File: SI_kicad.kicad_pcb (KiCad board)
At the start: 2 copper layers, 100 x 57 mm, 88 parts, among them J1 Conn_01x16_Female, J2 SCW_TERM_01x02, J3 Conn_02x05_Counter_Clockwise, J4 Conn_01x05_Male, J5 Conn_01x05_Female, J6 Conn_01x02, J7 Conn_01x02, Q1 BC549, Q2 BC557C, Q3 IRL7833, SW1 SW_Push, U1 STM32F103C8Tx, U2 AMS1117-3.3, U3 TPS5430DDA, U4 LM358, Y1 8M

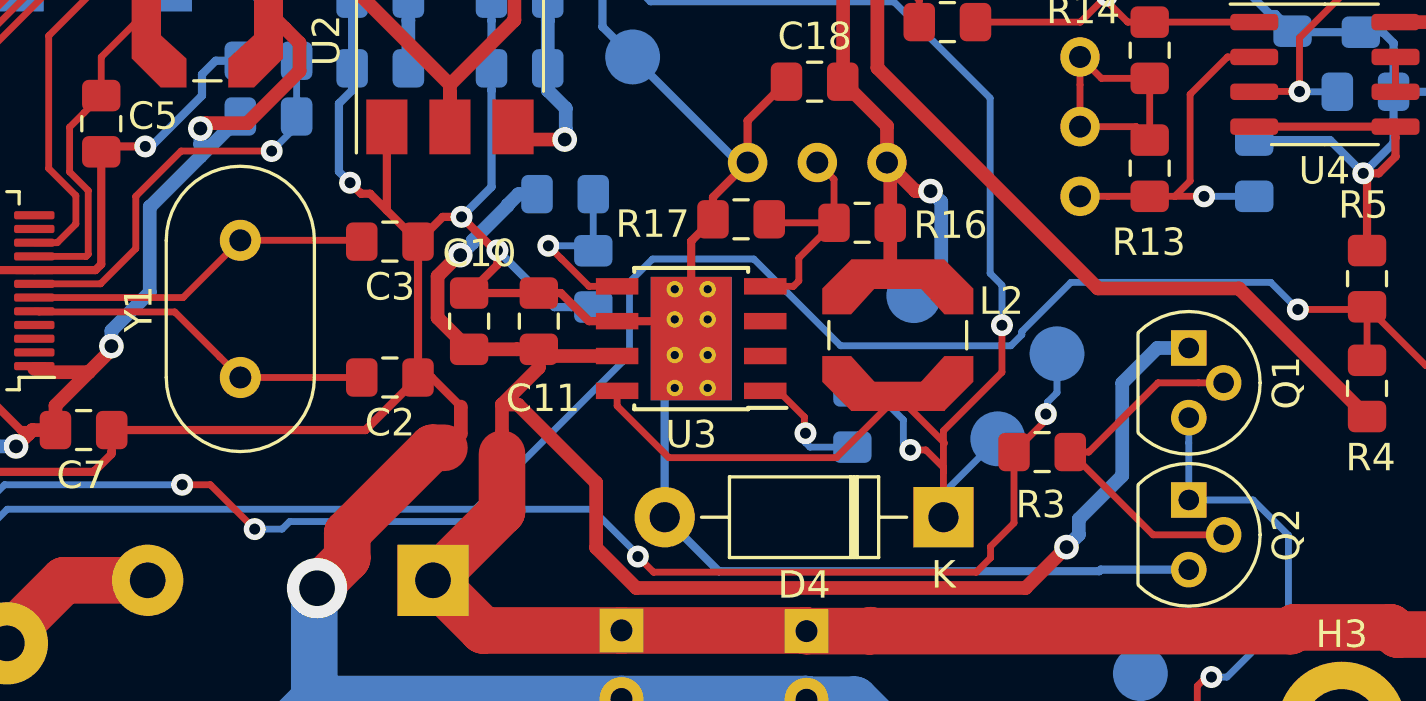
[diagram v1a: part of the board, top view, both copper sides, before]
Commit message: 1.2 Update schematic to kicad 6
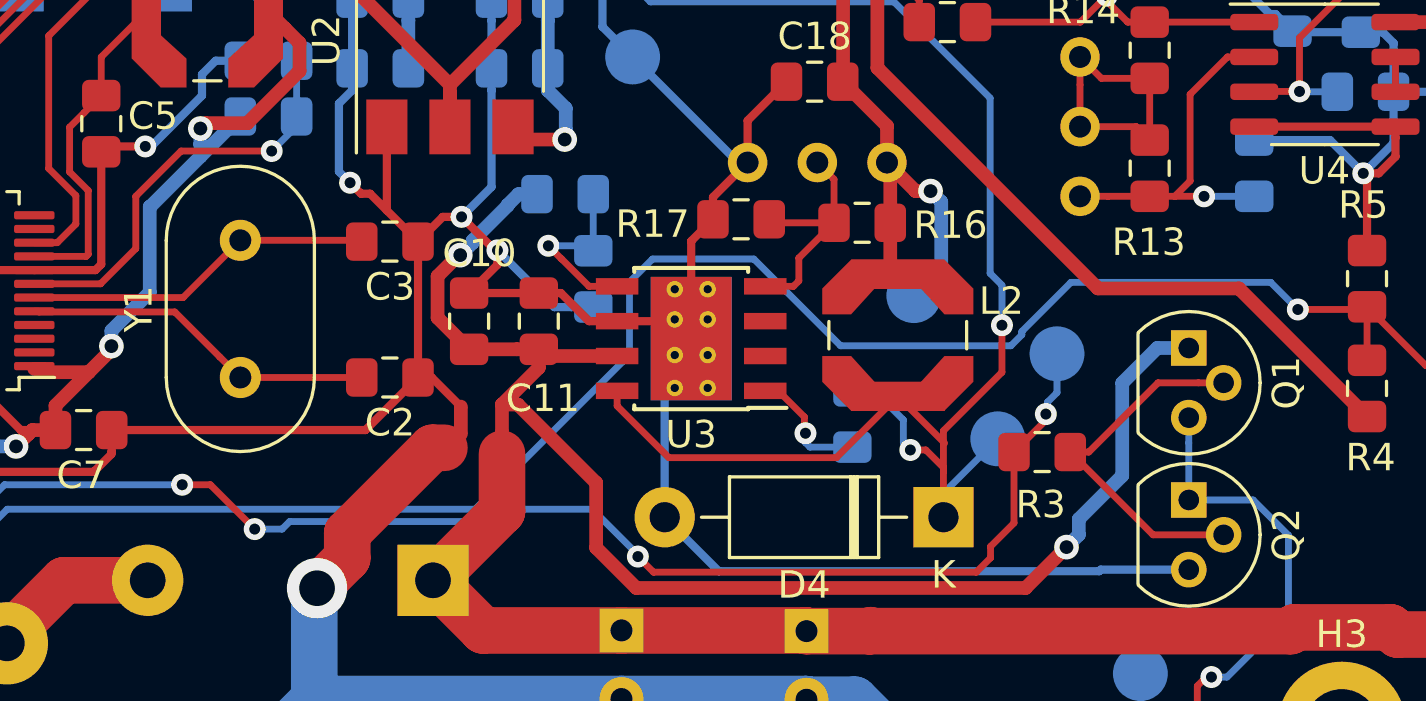
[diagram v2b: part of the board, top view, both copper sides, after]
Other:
- net class +28V removed
- net class Default removed
- net class GND removed
- net class VCC removed

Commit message: 2.0
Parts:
- removed D1: LED, LED_SMD:LED_0805_2012Metric_Pad1.15x1.40mm_HandSolder
- removed L3: INDUCTOR, Inductor_THT:L_Axial_L5.3mm_D2.2mm_P7.62mm_Horizontal_Vishay_IM-1
- removed NT2: Net-Tie_2, NetTie:NetTie-2_SMD_Pad0.5mm
- removed RV1: 1K, Potentiometer_THT:Potentiometer_Bourns_3296W_Vertical
- removed TP1, TP2, TP5, TP6, TP7, TP8, TP9: TestPoint, TestPoint:TestPoint_Pad_D2.0mm
- added C22: 2u, Capacitor_SMD:C_0805_2012Metric_Pad1.18x1.45mm_HandSolder, B.Cu at (103.1, 96.9)
- added C23: C_Polarized, Capacitor_THT:CP_Radial_D6.3mm_P2.50mm, B.Cu at (162.1, 107.5)
- added C24: 10n, Capacitor_SMD:C_0805_2012Metric_Pad1.18x1.45mm_HandSolder, B.Cu at (171.3, 90.4)
- added C25: 100n, Capacitor_SMD:C_0805_2012Metric_Pad1.18x1.45mm_HandSolder, B.Cu at (171.2, 92.2)
- added C26: 4.7u, Capacitor_SMD:CP_Elec_5x5.4, B.Cu at (153.0, 94.2)
- added C27: 100n, Capacitor_SMD:C_0805_2012Metric_Pad1.18x1.45mm_HandSolder, F.Cu at (184.1, 91.6)
- added C28: 100n, Capacitor_SMD:C_0805_2012Metric_Pad1.18x1.45mm_HandSolder, F.Cu at (158.4, 91.6)
- added C29: 100n, Capacitor_SMD:C_0805_2012Metric_Pad1.18x1.45mm_HandSolder, F.Cu at (152.6, 84.2)
- added C30: 100n, Capacitor_SMD:C_0805_2012Metric_Pad1.18x1.45mm_HandSolder, F.Cu at (149.0, 84.2)
- added C31: 10n, Capacitor_SMD:C_0805_2012Metric_Pad1.18x1.45mm_HandSolder, F.Cu at (178.5, 102.2)
- added C32: 100n, Capacitor_SMD:C_0805_2012Metric_Pad1.18x1.45mm_HandSolder, F.Cu at (175.9, 102.3)
- added C33: 10n, Capacitor_SMD:C_0805_2012Metric_Pad1.18x1.45mm_HandSolder, F.Cu at (167.6, 102.2)
- added C34: 100n, Capacitor_SMD:C_0805_2012Metric_Pad1.18x1.45mm_HandSolder, F.Cu at (165.0, 102.2)
- added D5: 1N4001, Diode_SMD:D_SMA, F.Cu at (185.0, 102.5)
- added D6: 1N4001, Diode_SMD:D_SMA, F.Cu at (185.3, 115.1)
- added J10: Conn_01x02, Connector_PinHeader_2.54mm:PinHeader_1x02_P2.54mm_Vertical, B.Cu at (169.9, 82.5)
- added J11: Conn_01x02, Connector_PinHeader_2.54mm:PinHeader_1x02_P2.54mm_Vertical, B.Cu at (162.2, 82.5)
- added J12: Conn_01x02, Connector_PinHeader_2.54mm:PinHeader_1x02_P2.54mm_Vertical, B.Cu at (172.9, 80.0)
- added J13: Conn_01x02, Connector_PinHeader_2.54mm:PinHeader_1x02_P2.54mm_Vertical, B.Cu at (158.9, 80.0)
- added J8: Conn_01x04, Connector_JST:JST_EH_B4B-EH-A_1x04_P2.50mm_Vertical, B.Cu at (99.4, 86.7)
- added J9: Conn_01x04_Female, Connector_JST:JST_EH_B4B-EH-A_1x04_P2.50mm_Vertical, B.Cu at (190.6, 110.5)
- added Q4: 2N7002, Package_TO_SOT_SMD:SOT-23, F.Cu at (110.6, 87.5)
- added Q5: IRL7833, Package_TO_SOT_THT:TO-220-3_Vertical, B.Cu at (176.7, 121.8)
- added Q6: 2N7002, Package_TO_SOT_SMD:SOT-23, F.Cu at (126.0, 149.7)
- added R18: 100R, Resistor_SMD:R_0805_2012Metric_Pad1.20x1.40mm_HandSolder, F.Cu at (146.7, 100.3)
- added R19: 100R, Resistor_SMD:R_0805_2012Metric_Pad1.20x1.40mm_HandSolder, F.Cu at (146.7, 102.9)
- added R20: 100R, Resistor_SMD:R_0805_2012Metric_Pad1.20x1.40mm_HandSolder, F.Cu at (159.1, 100.3)
- added R21: 100R, Resistor_SMD:R_0805_2012Metric_Pad1.20x1.40mm_HandSolder, F.Cu at (159.1, 102.6)
- added R22: 9K, Resistor_SMD:R_0805_2012Metric_Pad1.20x1.40mm_HandSolder, F.Cu at (121.7, 74.9)
- added R23: 100k, Resistor_SMD:R_0805_2012Metric_Pad1.20x1.40mm_HandSolder, F.Cu at (118.5, 83.4)
- added R24: 10k, Resistor_SMD:R_0805_2012Metric_Pad1.20x1.40mm_HandSolder, F.Cu at (167.3, 82.5)
- added R25: 10k, Resistor_SMD:R_0805_2012Metric_Pad1.20x1.40mm_HandSolder, F.Cu at (164.8, 82.5)
- added R26: 100k, Resistor_SMD:R_0805_2012Metric_Pad1.20x1.40mm_HandSolder, F.Cu at (176.1, 82.2)
- added R27: 100k, Resistor_SMD:R_0805_2012Metric_Pad1.20x1.40mm_HandSolder, F.Cu at (155.3, 82.2)
- added R28: 1k, Resistor_SMD:R_0805_2012Metric_Pad1.20x1.40mm_HandSolder, F.Cu at (179.9, 87.7)
- added R29: 1k, Resistor_SMD:R_0805_2012Metric_Pad1.20x1.40mm_HandSolder, F.Cu at (162.5, 87.7)
- added R30: R, Resistor_SMD:R_0805_2012Metric_Pad1.20x1.40mm_HandSolder, F.Cu at (182.0, 91.6)
- added R31: R, Resistor_SMD:R_0805_2012Metric_Pad1.20x1.40mm_HandSolder, F.Cu at (160.5, 91.6)
- added R32: 100k, Resistor_SMD:R_0805_2012Metric_Pad1.20x1.40mm_HandSolder, F.Cu at (179.8, 98.6)
- added R33: 100k, Resistor_SMD:R_0805_2012Metric_Pad1.20x1.40mm_HandSolder, F.Cu at (162.8, 98.6)
- added R34: 470R, Resistor_SMD:R_0805_2012Metric_Pad1.20x1.40mm_HandSolder, F.Cu at (145.5, 87.7)
- added R35: 470R, Resistor_SMD:R_0805_2012Metric_Pad1.20x1.40mm_HandSolder, F.Cu at (145.5, 85.5)
- added R36: 1k, Resistor_SMD:R_0805_2012Metric_Pad1.20x1.40mm_HandSolder, F.Cu at (176.0, 92.5)
- added R37: 16k, Resistor_SMD:R_0805_2012Metric_Pad1.20x1.40mm_HandSolder, F.Cu at (176.0, 96.4)
- added R38: 1k, Resistor_SMD:R_0805_2012Metric_Pad1.20x1.40mm_HandSolder, F.Cu at (166.4, 92.5)
- added R39: 16k, Resistor_SMD:R_0805_2012Metric_Pad1.20x1.40mm_HandSolder, F.Cu at (166.4, 96.4)
- added R40: 100k, Resistor_SMD:R_0805_2012Metric_Pad1.20x1.40mm_HandSolder, F.Cu at (113.9, 83.4)
- added R41: 100k, Resistor_SMD:R_0805_2012Metric_Pad1.20x1.40mm_HandSolder, F.Cu at (109.3, 83.4)
- added R42: 100, Resistor_SMD:R_0805_2012Metric_Pad1.20x1.40mm_HandSolder, F.Cu at (109.9, 146.0)
- added R43: 100k, Resistor_SMD:R_0805_2012Metric_Pad1.20x1.40mm_HandSolder, F.Cu at (116.4, 149.7)
- added TP12: TestPoint, TestPoint:TestPoint_Pad_D2.0mm, F.Cu at (218.0, 147.8)
- added TP13: TestPoint, TestPoint:TestPoint_Pad_D2.0mm, F.Cu at (214.0, 147.8)
- added TP17: TestPoint, TestPoint:TestPoint_Pad_D2.0mm, F.Cu at (209.4, 153.8)
- added TP18: TestPoint, TestPoint:TestPoint_Pad_D2.0mm, F.Cu at (205.4, 153.8)
- added U5: LM324A, Package_SO:SO-14_3.9x8.65mm_P1.27mm, F.Cu at (171.2, 91.3)
- added U6: L78L12_SOT89, Package_TO_SOT_SMD:SOT-89-3, F.Cu at (171.7, 101.7)
- BZ1, TP4: moved to F.Cu
- C1: value 100n -> 22p; footprint Capacitor_SMD:C_0805_2012Metric_Pad1.15x1.40mm_HandSolder -> Capacitor_SMD:C_0805_2012Metric_Pad1.18x1.45mm_HandSolder
- C10, C14, C20, C5: value 10n -> 100n; footprint Capacitor_SMD:C_0805_2012Metric_Pad1.15x1.40mm_HandSolder -> Capacitor_SMD:C_0805_2012Metric_Pad1.18x1.45mm_HandSolder
- C11, C17, C7: footprint Capacitor_SMD:C_0805_2012Metric_Pad1.15x1.40mm_HandSolder -> Capacitor_SMD:C_0805_2012Metric_Pad1.18x1.45mm_HandSolder
- C12: value 10n -> 100n; footprint Capacitor_SMD:C_0805_2012Metric_Pad1.15x1.40mm_HandSolder -> Capacitor_SMD:C_0805_2012Metric_Pad1.18x1.45mm_HandSolder; moved to F.Cu
- C13: footprint Capacitor_SMD:C_0805_2012Metric_Pad1.15x1.40mm_HandSolder -> Capacitor_SMD:C_0805_2012Metric_Pad1.18x1.45mm_HandSolder; moved to F.Cu
- C15, C19, C21: value 100n -> 10n; footprint Capacitor_SMD:C_0805_2012Metric_Pad1.15x1.40mm_HandSolder -> Capacitor_SMD:C_0805_2012Metric_Pad1.18x1.45mm_HandSolder
- C16: value 15p -> 10n; footprint Capacitor_SMD:C_0805_2012Metric_Pad1.15x1.40mm_HandSolder -> Capacitor_SMD:C_0805_2012Metric_Pad1.18x1.45mm_HandSolder
- C18, C4, C6: footprint Capacitor_SMD:C_0805_2012Metric_Pad1.15x1.40mm_HandSolder -> Capacitor_SMD:C_0805_2012Metric_Pad1.18x1.45mm_HandSolder; moved to B.Cu
- C2: value 22n -> 22p; footprint Capacitor_SMD:C_0805_2012Metric_Pad1.15x1.40mm_HandSolder -> Capacitor_SMD:C_0805_2012Metric_Pad1.18x1.45mm_HandSolder; moved to B.Cu
- C3: value 22n -> 10n; footprint Capacitor_SMD:C_0805_2012Metric_Pad1.15x1.40mm_HandSolder -> Capacitor_SMD:C_0805_2012Metric_Pad1.18x1.45mm_HandSolder; moved to B.Cu
- D3: footprint Diode_THT:D_DO-41_SOD81_P10.16mm_Horizontal -> Diode_SMD:D_SMA; moved to B.Cu
- D4: value 1N4001 -> 1N4007; footprint Diode_THT:D_DO-41_SOD81_P10.16mm_Horizontal -> Diode_SMD:D_SMA
- J2: footprint TerminalBlock:TerminalBlock_Altech_AK300-2_P5.00mm -> TerminalBlock_Phoenix:TerminalBlock_Phoenix_MKDS-1,5-2-5.08_1x02_P5.08mm_Horizontal
- J4: value Conn_01x05_Male -> Conn_01x03_Female; footprint Connector_PinHeader_2.54mm:PinHeader_1x05_P2.54mm_Horizontal -> Connector_JST:JST_EH_B3B-EH-A_1x03_P2.50mm_Vertical
- J5: value Conn_01x05_Female -> Conn_01x04_Female; footprint Connector_PinSocket_2.54mm:PinSocket_1x05_P2.54mm_Vertical -> Connector_JST:JST_EH_B4B-EH-A_1x04_P2.50mm_Vertical
- J6: value Conn_01x02 -> Conn_01x04; footprint Connector_PinHeader_2.54mm:PinHeader_1x02_P2.54mm_Vertical -> Connector_JST:JST_EH_B4B-EH-A_1x04_P2.50mm_Vertical
- J7: value Conn_01x02 -> Conn_01x05_Male; footprint Connector_PinHeader_2.54mm:PinHeader_1x02_P2.54mm_Vertical -> Connector_JST:JST_EH_B5B-EH-A_1x05_P2.50mm_Vertical
- L1: footprint Inductor_SMD:L_Coilcraft_LPS5030 -> Inductor_SMD:L_0805_2012Metric; moved to B.Cu
- L2: footprint Inductor_SMD:L_Coilcraft_LPS5030 -> Inductor_SMD:L_Coilcraft_LPS4018; moved to B.Cu
- Q1: value BC549 -> 2N7002; footprint Package_TO_SOT_THT:TO-92 -> Package_TO_SOT_SMD:SOT-23
- Q2: value BC557C -> 2N7002; footprint Package_TO_SOT_THT:TO-92 -> Package_TO_SOT_SMD:SOT-23
- R1: value 10k -> 1K; footprint Resistor_SMD:R_0805_2012Metric_Pad1.15x1.40mm_HandSolder -> Resistor_SMD:R_0805_2012Metric_Pad1.20x1.40mm_HandSolder; moved to F.Cu
- R10: value 10k -> 100; footprint Resistor_SMD:R_0805_2012Metric_Pad1.15x1.40mm_HandSolder -> Resistor_SMD:R_0805_2012Metric_Pad1.20x1.40mm_HandSolder; moved to B.Cu
- R11: value 100k -> 100; footprint Resistor_SMD:R_0805_2012Metric_Pad1.15x1.40mm_HandSolder -> Resistor_SMD:R_0805_2012Metric_Pad1.20x1.40mm_HandSolder
- R12: value 1k -> 10k; footprint Resistor_SMD:R_0805_2012Metric_Pad1.15x1.40mm_HandSolder -> Resistor_SMD:R_0805_2012Metric_Pad1.20x1.40mm_HandSolder; moved to F.Cu
- R13: value R -> 10k; footprint Resistor_SMD:R_0805_2012Metric_Pad1.15x1.40mm_HandSolder -> Resistor_SMD:R_0805_2012Metric_Pad1.20x1.40mm_HandSolder; moved to B.Cu
- R14: value 100k -> 16k; footprint Resistor_SMD:R_0805_2012Metric_Pad1.15x1.40mm_HandSolder -> Resistor_SMD:R_0805_2012Metric_Pad1.20x1.40mm_HandSolder; moved to B.Cu
- R15: value 470R -> 1.6k; footprint Resistor_SMD:R_0805_2012Metric_Pad1.15x1.40mm_HandSolder -> Resistor_SMD:R_0805_2012Metric_Pad1.20x1.40mm_HandSolder; moved to B.Cu
- R16: value 15k -> 10k; footprint Resistor_SMD:R_0805_2012Metric_Pad1.15x1.40mm_HandSolder -> Resistor_SMD:R_0805_2012Metric_Pad1.20x1.40mm_HandSolder; moved to B.Cu
- R17: value 33k -> 3.3k; footprint Resistor_SMD:R_0805_2012Metric_Pad1.15x1.40mm_HandSolder -> Resistor_SMD:R_0805_2012Metric_Pad1.20x1.40mm_HandSolder; moved to B.Cu
- R2: value 220R -> 100; footprint Resistor_SMD:R_0805_2012Metric_Pad1.15x1.40mm_HandSolder -> Resistor_SMD:R_0805_2012Metric_Pad1.20x1.40mm_HandSolder; moved to F.Cu
- R3: value 100R -> 100; footprint Resistor_SMD:R_0805_2012Metric_Pad1.15x1.40mm_HandSolder -> Resistor_SMD:R_0805_2012Metric_Pad1.20x1.40mm_HandSolder
- R4: value 220R -> 100; footprint Resistor_SMD:R_0805_2012Metric_Pad1.15x1.40mm_HandSolder -> Resistor_SMD:R_0805_2012Metric_Pad1.20x1.40mm_HandSolder
- R5: value 220R -> 10k; footprint Resistor_SMD:R_0805_2012Metric_Pad1.15x1.40mm_HandSolder -> Resistor_SMD:R_0805_2012Metric_Pad1.20x1.40mm_HandSolder
- R6: value 15k -> 10k; footprint Resistor_SMD:R_0805_2012Metric_Pad1.15x1.40mm_HandSolder -> Resistor_SMD:R_0805_2012Metric_Pad1.20x1.40mm_HandSolder; moved to F.Cu
- R7: value 5k -> 10k; footprint Resistor_SMD:R_0805_2012Metric_Pad1.15x1.40mm_HandSolder -> Resistor_SMD:R_0805_2012Metric_Pad1.20x1.40mm_HandSolder; moved to F.Cu
- R8: value 100R -> 10k; footprint Resistor_SMD:R_0805_2012Metric_Pad1.15x1.40mm_HandSolder -> Resistor_SMD:R_0805_2012Metric_Pad1.20x1.40mm_HandSolder
- R9: value 100k -> 10k; footprint Resistor_SMD:R_0805_2012Metric_Pad1.15x1.40mm_HandSolder -> Resistor_SMD:R_0805_2012Metric_Pad1.20x1.40mm_HandSolder
- RV3: value 50k -> 500k
- U2, U3: moved to B.Cu
- U4: value LM358 -> IR4427; footprint Package_SO:SO-8_3.9x4.9mm_P1.27mm -> Package_SO:SOIC-8_3.9x4.9mm_P1.27mm
- moved H9 122.6 mm to (48.4, 109.0)
- moved TP10 89.6 mm to (255.2, 77.5)
- moved R10 84.4 mm to (104.2, 86.7), turned to 180 degrees
- moved TP3 83.4 mm to (104.2, 100.8), turned to 180 degrees
- moved R11 82.6 mm to (104.2, 81.7)
- moved C21 73.5 mm to (108.9, 98.2), turned to 0 degrees
- moved R4 73.2 mm to (111.6, 83.4)
- moved D3 70.0 mm to (117.7, 99.4), turned to 0 degrees
- moved C17 66.6 mm to (117.5, 95.8), turned to -90 degrees
- moved R5 63.7 mm to (119.8, 91.8), turned to 90 degrees
- moved R14 63.6 mm to (112.2, 90.1), turned to -90 degrees
- moved J6 63.6 mm to (135.3, 122.8), turned to 180 degrees
- moved Q2 63.6 mm to (114.9, 87.5)
- moved R16 61.0 mm to (104.1, 93.6), turned to -90 degrees
- moved R15 59.3 mm to (109.2, 89.2)
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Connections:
- BZ1 pad 1: Buzzer -> +3V3
- BZ1 pad 2: GND -> Net-(BZ1-+)
- C1 pad 1: NRST -> GND
- C1 pad 2: GND -> Net-(U1-PD0)
- C10 pad 1: +24V -> ENCODER_DT
- C11 pad 1: +24V -> ENCODER_CLK
- C12 pad 1: +5V -> Net-(J8-Pin_1)
- C13 pad 1: +5V -> Net-(J8-Pin_3)
- C14 pad 1: +3V3 -> NRST
- C15 pad 1: +3V3 -> +24V
- C16 pad 1: Net-(C16-Pad1) -> +5V
- C16 pad 2: Net-(C16-Pad2) -> GND
- C17 pad 1: Net-(C17-Pad1) -> +24V
- C18 pad 1: GND -> +5V
- C18 pad 2: +5V -> GND
- C19 pad 1: Net-(C19-Pad1) -> +3V3
- C2 pad 2: Net-(C2-Pad2) -> Net-(U1-PD1)
- C20 pad 1: +5V -> +3V3
- C21 pad 1: +5V -> Net-(U3-BOOT)
- C21 pad 2: GND -> Net-(D3-K)
- C3 pad 1: GND -> +3V3
- C3 pad 2: Net-(C3-Pad2) -> GND
- C4 pad 1: +3V3 -> Net-(U1-VDDA)
- C5 pad 1: Net-(C5-Pad1) -> +3V3
- C7 pad 1: +3V3 -> ENCODER_SW
- C8 pad 1: SI_24_1 -> SI_24_1_I
- C9 pad 1: SI_24_1 -> SI_24_1_I
- D2 pad 1: SI_24_1 -> SI_24_1_I
- D3 pad 1: SI_24_1 -> Net-(D3-K)
- D3 pad 2: SI_24_2 -> GND
- D4 pad 1: Net-(C16-Pad2) -> +24V
- D4 pad 2: GND -> SI_24_1_I
- J1 pad 10: (no net) -> unconnected-(J1-Pin_10-Pad10)
- J1 pad 7: (no net) -> unconnected-(J1-Pin_7-Pad7)
- J1 pad 8: (no net) -> unconnected-(J1-Pin_8-Pad8)
- J1 pad 9: (no net) -> unconnected-(J1-Pin_9-Pad9)
- J4 pad 1: ENCODER_CLK -> GND
- J4 pad 2: ENCODER_DT -> USART1_RX
- J4 pad 3: ENCODER_SW -> USART1_TX
- J5 pad 1: Iron_IN -> GND
- J5 pad 2: GND -> Net-(J10-Pin_1)
- J5 pad 3: Net-(J5-Pad3) -> SI_24_1_I
- J5 pad 4: SI_24_1 -> SI_24_2_I
- J6 pad 1: Net-(J5-Pad3) -> +5V
- J6 pad 2: Net-(C17-Pad1) -> Net-(J6-Pin_2)
- J7 pad 1: Net-(C17-Pad1) -> Net-(J7-Pin_1)
- J7 pad 2: Net-(J7-Pad2) -> Net-(J7-Pin_2)
- L1 pad 1: Net-(C5-Pad1) -> Net-(U1-VDDA)
- L2 pad 1: Net-(C16-Pad2) -> Net-(D3-K)
- Q1 pad 1: +24V -> Net-(Q1-G)
- Q1 pad 2: Net-(Q1-Pad2) -> GND
- Q1 pad 3: Net-(Q1-Pad3) -> LED3_P
- Q2 pad 1: Net-(Q1-Pad3) -> Net-(Q2-G)
- Q2 pad 2: Net-(Q1-Pad2) -> GND
- Q2 pad 3: GND -> LED2_P
- Q3 pad 1: Net-(Q3-Pad1) -> P_PWM1
- Q3 pad 2: SI_24_2 -> SI_24_2_I
- R1 pad 1: +3V3 -> +5V
- R1 pad 2: NRST -> LCD_R
- R10 pad 1: Net-(C17-Pad1) -> Button1
- R10 pad 2: Net-(J5-Pad3) -> Net-(J8-Pin_1)
- R11 pad 1: Net-(J7-Pad2) -> Button2
- R11 pad 2: +5V -> Net-(J8-Pin_3)
- R12 pad 1: Net-(R12-Pad1) -> ENCODER_CLK
- R12 pad 2: GND -> Net-(J7-Pin_1)
- R13 pad 1: Net-(R12-Pad1) -> +3V3
- R13 pad 2: Net-(R13-Pad2) -> NRST
- R14 pad 1: Net-(R13-Pad2) -> +24V
- R14 pad 2: Net-(C19-Pad1) -> Net-(U3-EN)
- R15 pad 1: Net-(C19-Pad1) -> Net-(U3-EN)
- R15 pad 2: AIN0 -> GND
- R16 pad 1: Net-(R16-Pad1) -> Net-(U3-VSENSE)
- R17 pad 2: Net-(R16-Pad1) -> Net-(U3-VSENSE)
- R2 pad 1: LED -> LED1
- R2 pad 2: Net-(D1-Pad2) -> Net-(Q1-G)
- R3 pad 1: PWM1 -> LED2
- R3 pad 2: Net-(Q1-Pad2) -> Net-(Q2-G)
- R4 pad 1: Iron_IN -> LED3
- R4 pad 2: +3V3 -> Net-(Q4-G)
- R5 pad 1: GND -> Net-(J6-Pin_2)
- R5 pad 2: Iron_IN -> LED3_P
- R6 pad 1: +24V -> Net-(J6-Pin_3)
- R6 pad 2: Net-(R6-Pad2) -> LED2_P
- R7 pad 1: Net-(R6-Pad2) -> Net-(J6-Pin_4)
- R7 pad 2: GND -> LED1_P
- R8 pad 1: Net-(Q1-Pad3) -> ENCODER_SW
- R8 pad 2: Net-(Q3-Pad1) -> Net-(J7-Pin_3)
- R9 pad 1: GND -> ENCODER_DT
- R9 pad 2: Net-(Q3-Pad1) -> Net-(J7-Pin_2)
- RV2 pad 1: Net-(R12-Pad1) -> Net-(U5B--)
- RV2 pad 2: Net-(R13-Pad2) -> Net-(R30-Pad2)
- RV2 pad 3: Net-(R13-Pad2) -> unconnected-(RV2-Pad3)
- RV3 pad 1: GND -> Net-(U5C--)
- RV3 pad 2: Net-(R16-Pad1) -> Net-(R31-Pad2)
- RV3 pad 3: +5V -> unconnected-(RV3-Pad3)
- TP10 pad 1: +5V -> Net-(J10-Pin_1)
- TP3 pad 1: Net-(J5-Pad3) -> +5V
- U1 pad 11: (no net) -> AIN1
- U1 pad 12: (no net) -> AIN2
- U1 pad 13: (no net) -> AIN3
- U1 pad 2: (no net) -> unconnected-(U1-PC13-Pad2)
- U1 pad 20: LED -> unconnected-(U1-PB2-Pad20)
- U1 pad 21: (no net) -> PWM2
- U1 pad 22: (no net) -> unconnected-(U1-PB11-Pad22)
- U1 pad 25: (no net) -> LED1
- U1 pad 26: Buzzer -> LED2
- U1 pad 27: (no net) -> Button2
- U1 pad 28: (no net) -> Button1
- U1 pad 3: (no net) -> unconnected-(U1-PC14-Pad3)
- U1 pad 32: (no net) -> LED3
- U1 pad 33: Iron_IN -> unconnected-(U1-PA12-Pad33)
- U1 pad 4: (no net) -> unconnected-(U1-PC15-Pad4)
- U1 pad 40: (no net) -> unconnected-(U1-PB4-Pad40)
- U1 pad 41: (no net) -> unconnected-(U1-PB5-Pad41)
- U1 pad 42: (no net) -> USART1_TX
- U1 pad 43: (no net) -> USART1_RX
- U1 pad 44: (no net) -> unconnected-(U1-BOOT0-Pad44)
- U1 pad 45: (no net) -> Buzzer
- U1 pad 46: (no net) -> unconnected-(U1-PB9-Pad46)
- U1 pad 5: Net-(C2-Pad2) -> Net-(U1-PD0)
- U1 pad 6: Net-(C3-Pad2) -> Net-(U1-PD1)
- U1 pad 9: Net-(C5-Pad1) -> Net-(U1-VDDA)
- U3 pad 1: Net-(C16-Pad1) -> Net-(U3-BOOT)
- U3 pad 2: (no net) -> unconnected-(U3-NC-Pad2)
- U3 pad 3: (no net) -> unconnected-(U3-NC-Pad3)
- U3 pad 4: Net-(R16-Pad1) -> Net-(U3-VSENSE)
- U3 pad 5: Net-(R6-Pad2) -> Net-(U3-EN)
- U3 pad 8: Net-(C16-Pad2) -> Net-(D3-K)
- U4 pad 1: Net-(C19-Pad1) -> unconnected-(U4-NC-Pad1)
- U4 pad 2: Net-(R12-Pad1) -> Net-(U4-IN_A)
- U4 pad 3: Net-(C17-Pad1) -> GND
- U4 pad 4: GND -> Net-(U4-IN_B)
- U4 pad 5: GND -> Net-(U4-OUT_B)
- U4 pad 6: Net-(U4-Pad6) -> +12V
- U4 pad 7: Net-(U4-Pad6) -> Net-(U4-OUT_A)
- U4 pad 8: +5V -> unconnected-(U4-NC-Pad8)
- Y1 pad 1: Net-(C2-Pad2) -> Net-(U1-PD0)
- Y1 pad 2: Net-(C3-Pad2) -> Net-(U1-PD1)
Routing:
- net Iron_IN: track 93.2 -> 0.00 mm, vias 2 -> 0
- net GND: track 397.1 -> 320.6 mm, vias 6 -> 10
- net Net-(C16-Pad2): track 56.2 -> 0.00 mm, vias 2 -> 0
- net SI_24_1: track 54.6 -> 0.00 mm
- net PWM1: track 54.9 -> 1.79 mm, vias 5 -> 1
- net SI_24_1_I: track 0.00 -> 53.0 mm
- net ENCODER_SW: track 21.8 -> 74.7 mm, vias 1 -> 4
- net +3V3: track 166.2 -> 114.5 mm, vias 8 -> 6
- net ENCODER_CLK: track 21.8 -> 72.7 mm, vias 1 -> 6
- net ENCODER_DT: track 22.0 -> 72.1 mm, vias 1 -> 6
- net SI_24_2_I: track 0.00 -> 41.1 mm, vias 0 -> 1
- net +24V: track 51.3 -> 11.1 mm, vias 2 -> 0
- net AIN0: track 49.6 -> 11.2 mm, vias 1 -> 0
- net USART1_RX: track 0.00 -> 36.0 mm
- net USART1_TX: track 0.00 -> 36.0 mm
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- removed copper zone on B.Cu, net GND
- removed copper zone on F.Cu, net GND
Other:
- board text added: "03.2023"
- board text added: "Ver 2.0"
- board text removed: "10.2019"
- board text removed: "Ver 1.1"
